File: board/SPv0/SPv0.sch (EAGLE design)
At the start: 53 parts, among them IC1 S34ML0XG1, IC2 F55[0/1]X---PT48, IC3 LM339D, Q1 12MHz, T1 n3904, T2 n3904, T3 n3906, T4 n3906, T5 n3906

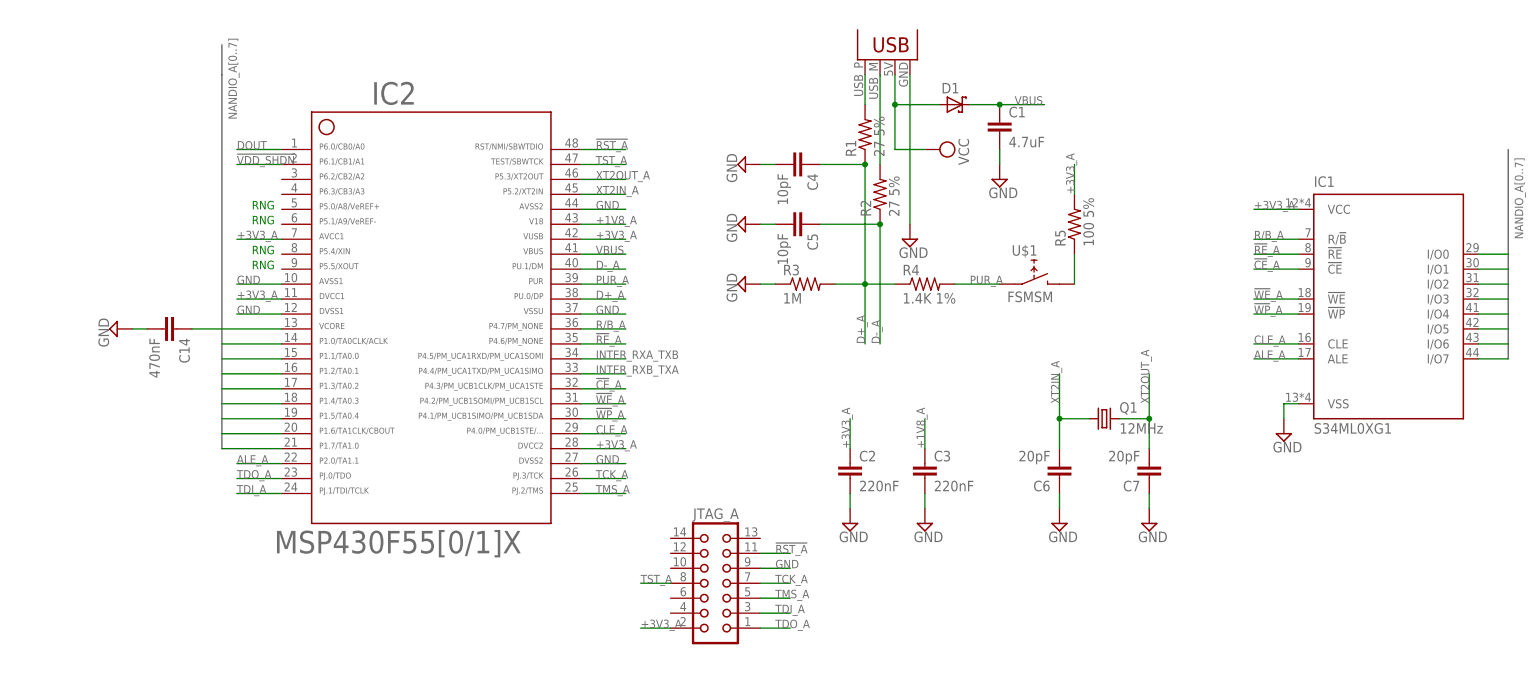
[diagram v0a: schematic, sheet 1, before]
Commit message: added own footprints for 0805 parts reorganizing board somewhat
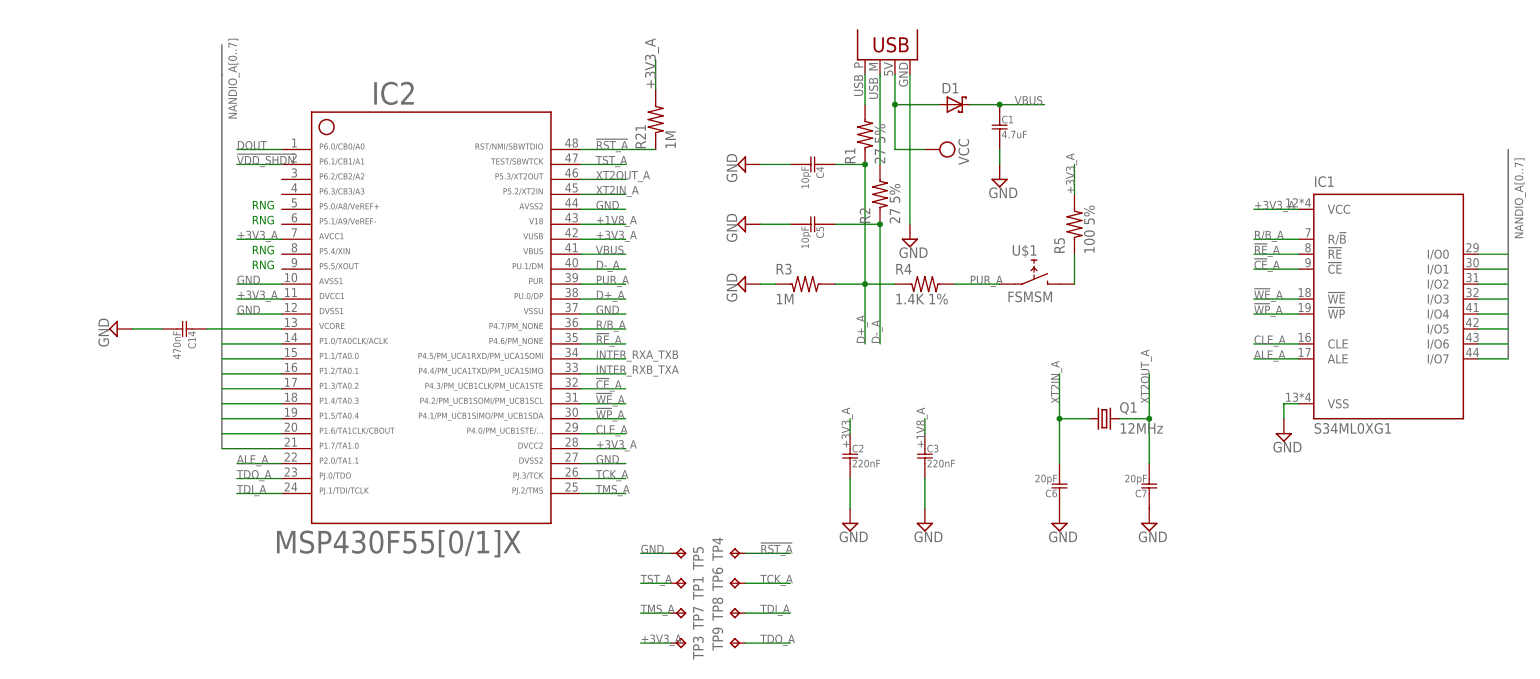
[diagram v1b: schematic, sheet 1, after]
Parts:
- removed JTAG_A: (no value), con-harting:CON14
- added R21: 1M, Passives:R0805
- added TP1, TP3, TP4, TP5, TP6, TP7, TP8, TP9: TPTP08SQ, testpad:TPTP08SQ
- C1, C14, C2, C3, C4, C5, C6, C7: device rcl:C-EUC0805 -> Passives:C0805
- Q1: device Passives:CRYSTAL -> Passives:CRYSTALCSM-3X
- R1, R2, R3, R4, R5: device rcl:R-US_R0805 -> Passives:R0805
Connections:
- net !RST_A!: now also R21.1, TP4.TP; no longer JTAG_A.11
- net +3V3_A: now also R21.2, TP3.TP; no longer JTAG_A.2
- net GND: now also TP5.TP; no longer JTAG_A.9
- net TCK_A: now also TP6.TP; no longer JTAG_A.7
- net TDI_A: now also TP8.TP; no longer JTAG_A.3
- net TDO_A: now also TP9.TP; no longer JTAG_A.1
- net TMS_A: now also TP7.TP; no longer JTAG_A.5
- net TST_A: now also TP1.TP; no longer JTAG_A.8

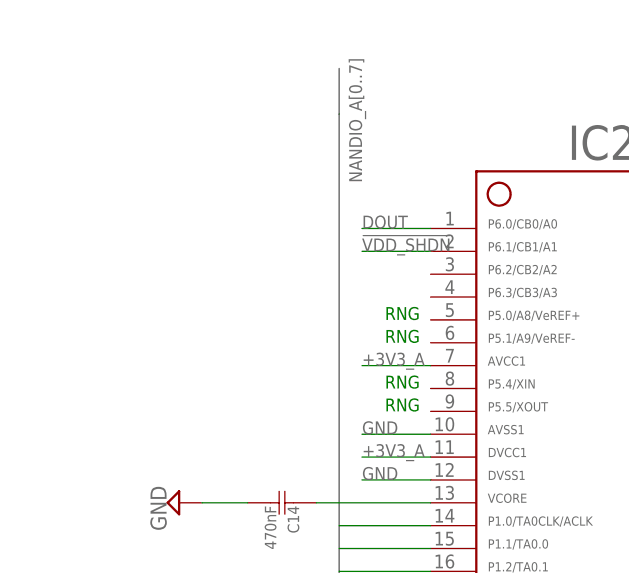
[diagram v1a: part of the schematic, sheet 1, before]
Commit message: adding primordial hwrng support added leds to library, board
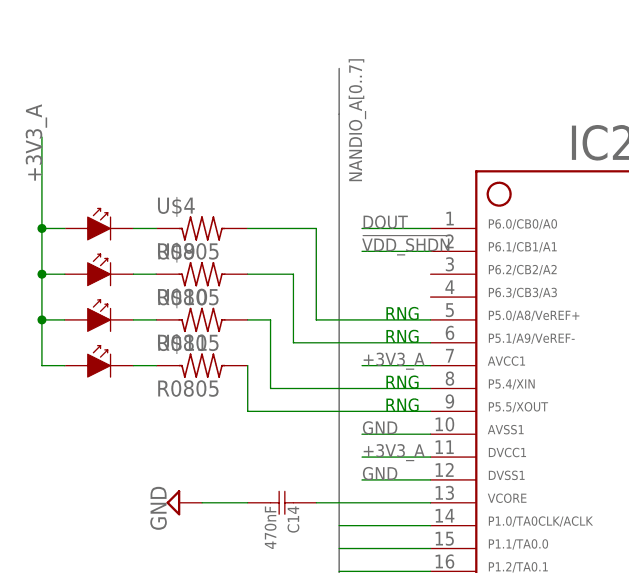
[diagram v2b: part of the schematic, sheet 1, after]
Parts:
- added U$10, U$11, U$4, U$9: R0805, Passives:R0805
- added U$5, U$6, U$7, U$8: LED, Passives:LED
- D2, D3: value (none) -> 1n4148
- IC3: value LM339D -> TL084D; device linear:LM339D -> linear:TL084D
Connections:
- new net N$19: IC2.9, U$11.2
- new net N$22: U$10.1, U$7.CATHODE
- new net N$23: U$6.CATHODE, U$9.1
- new net N$24: U$4.1, U$5.CATHODE
- new net N$25: U$11.1, U$8.CATHODE
- new net N$26: IC2.8, U$10.2
- new net N$27: IC2.6, U$9.2
- new net N$28: IC2.5, U$4.2
- net +3V3_A: now also U$5.ANODE, U$6.ANODE, U$7.ANODE, U$8.ANODE
- net GND: now also IC3P.V-; no longer IC3P.GND
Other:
- moved on the sheet: IC3C
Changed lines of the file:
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@@
 <part name="R7" library="rcl" deviceset="R-US_" device="R0603" value="1M"/>
 <part name="SUPPLY11" library="supply2" deviceset="GND" device=""/>
-<part name="IC3" library="linear" deviceset="LM339" device="D"/>
+<part name="IC3" library="linear" deviceset="TL084" device="D"/>
 <part name="C8" library="rcl" deviceset="C-EU" device="C0805" value="0.47u"/>
 <part name="C9" library="rcl" deviceset="C-EU" device="C0805" value="0.47u"/>
@@
 <part name="R16" library="rcl" deviceset="R-US_" device="R0603" value="5K"/>
 <part name="R17" library="rcl" deviceset="R-US_" device="R0603" value="5K"/>
-<part name="D2" library="zetex" deviceset="D" device="SOD323"/>
-<part name="D3" library="zetex" deviceset="D" device="SOD323"/>
+<part name="D2" library="zetex" deviceset="D" device="SOD323" value="1n4148"/>
+<part name="D3" library="zetex" deviceset="D" device="SOD323" value="1n4148"/>
 <part name="SUPPLY14" library="supply2" deviceset="GND" device=""/>
 <part name="SUPPLY15" library="supply2" deviceset="GND" device=""/>
@@
 <part name="TP9" library="testpad" deviceset="TP" device="TP08SQ"/>
 <part name="R21" library="Passives" deviceset="R" device="0805" value="1M"/>
+<part name="U$5" library="Passives" deviceset="LED" device=""/>
+<part name="U$6" library="Passives" deviceset="LED" device=""/>
+<part name="U$7" library="Passives" deviceset="LED" device=""/>
+<part name="U$8" library="Passives" deviceset="LED" device=""/>
+<part name="U$4" library="Passives" deviceset="R" device="0805"/>
+<part name="U$9" library="Passives" deviceset="R" device="0805"/>
+<part name="U$10" library="Passives" deviceset="R" device="0805"/>
+<part name="U$11" library="Passives" deviceset="R" device="0805"/>
 </parts>
 <sheets>
@@
 <instance part="TP9" gate="G$1" x="99.06" y="33.02" rot="R90"/>
 <instance part="R21" gate="G$1" x="86.36" y="121.92" rot="R90"/>
+<instance part="U$5" gate="G$1" x="-12.7" y="116.84"/>
+<instance part="U$6" gate="G$1" x="-12.7" y="111.76"/>
+<instance part="U$7" gate="G$1" x="-12.7" y="106.68"/>
+<instance part="U$8" gate="G$1" x="-12.7" y="101.6"/>
+<instance part="U$4" gate="G$1" x="-2.54" y="116.84"/>
+<instance part="U$9" gate="G$1" x="-2.54" y="111.76"/>
+<instance part="U$10" gate="G$1" x="-2.54" y="106.68"/>
+<instance part="U$11" gate="G$1" x="-2.54" y="101.6"/>
 </instances>
 <busses>
@@
 <wire x1="86.36" y1="127" x2="86.36" y2="132.08" width="0.1524" layer="91"/>
 <label x="86.36" y="127" size="1.778" layer="95" rot="R90"/>
+</segment>
+<segment>
+<pinref part="U$8" gate="G$1" pin="ANODE"/>
+<wire x1="-17.78" y1="101.6" x2="-20.32" y2="101.6" width="0.1524" layer="91"/>
+<wire x1="-20.32" y1="101.6" x2="-20.32" y2="106.68" width="0.1524" layer="91"/>
+<pinref part="U$5" gate="G$1" pin="ANODE"/>
+<wire x1="-20.32" y1="106.68" x2="-20.32" y2="111.76" width="0.1524" layer="91"/>
+<wire x1="-20.32" y1="111.76" x2="-20.32" y2="116.84" width="0.1524" layer="91"/>
+<wire x1="-20.32" y1="116.84" x2="-20.32" y2="127" width="0.1524" layer="91"/>
+<wire x1="-17.78" y1="116.84" x2="-20.32" y2="116.84" width="0.1524" layer="91"/>
+<junction x="-20.32" y="116.84"/>
+<pinref part="U$6" gate="G$1" pin="ANODE"/>
+<wire x1="-17.78" y1="111.76" x2="-20.32" y2="111.76" width="0.1524" layer="91"/>
+<junction x="-20.32" y="111.76"/>
+<pinref part="U$7" gate="G$1" pin="ANODE"/>
+<wire x1="-17.78" y1="106.68" x2="-20.32" y2="106.68" width="0.1524" layer="91"/>
+<junction x="-20.32" y="106.68"/>
+<label x="-20.32" y="121.92" size="1.778" layer="95" rot="R90"/>
 </segment>
 </net>
@@
 <wire x1="22.86" y1="114.3" x2="15.24" y2="114.3" width="0.1524" layer="91"/>
 <label x="15.24" y="114.3" size="1.4224" layer="95"/>
+</segment>
+</net>
+<net name="N$22" class="0">
+<segment>
+<pinref part="U$7" gate="G$1" pin="CATHODE"/>
+<pinref part="U$10" gate="G$1" pin="1"/>
+<wire x1="-10.16" y1="106.68" x2="-7.62" y2="106.68" width="0.1524" layer="91"/>
+</segment>
+</net>
+<net name="N$23" class="0">
+<segment>
+<pinref part="U$6" gate="G$1" pin="CATHODE"/>
+<pinref part="U$9" gate="G$1" pin="1"/>
+<wire x1="-10.16" y1="111.76" x2="-7.62" y2="111.76" width="0.1524" layer="91"/>
+</segment>
+</net>
+<net name="N$24" class="0">
+<segment>
+<pinref part="U$5" gate="G$1" pin="CATHODE"/>
+<pinref part="U$4" gate="G$1" pin="1"/>
+<wire x1="-10.16" y1="116.84" x2="-7.62" y2="116.84" width="0.1524" layer="91"/>
+</segment>
+</net>
+<net name="N$25" class="0">
+<segment>
+<pinref part="U$8" gate="G$1" pin="CATHODE"/>
+<pinref part="U$11" gate="G$1" pin="1"/>
+<wire x1="-10.16" y1="101.6" x2="-7.62" y2="101.6" width="0.1524" layer="91"/>
+</segment>
+</net>
+<net name="N$19" class="0">
+<segment>
+<pinref part="U$11" gate="G$1" pin="2"/>
+<wire x1="2.54" y1="101.6" x2="2.54" y2="96.52" width="0.1524" layer="91"/>
+<pinref part="IC2" gate="G$1" pin="9"/>
+<wire x1="2.54" y1="96.52" x2="22.86" y2="96.52" width="0.1524" layer="91"/>
+</segment>
+</net>
+<net name="N$26" class="0">
+<segment>
+<pinref part="IC2" gate="G$1" pin="8"/>
+<wire x1="22.86" y1="99.06" x2="5.08" y2="99.06" width="0.1524" layer="91"/>
+<wire x1="5.08" y1="99.06" x2="5.08" y2="106.68" width="0.1524" layer="91"/>
+<pinref part="U$10" gate="G$1" pin="2"/>
+<wire x1="5.08" y1="106.68" x2="2.54" y2="106.68" width="0.1524" layer="91"/>
+</segment>
+</net>
+<net name="N$27" class="0">
+<segment>
+<pinref part="U$9" gate="G$1" pin="2"/>
+<wire x1="2.54" y1="111.76" x2="7.62" y2="111.76" width="0.1524" layer="91"/>
+<wire x1="7.62" y1="111.76" x2="7.62" y2="104.14" width="0.1524" layer="91"/>
+<pinref part="IC2" gate="G$1" pin="6"/>
+<wire x1="7.62" y1="104.14" x2="22.86" y2="104.14" width="0.1524" layer="91"/>
+</segment>
+</net>
+<net name="N$28" class="0">
+<segment>
+<pinref part="U$4" gate="G$1" pin="2"/>
+<wire x1="2.54" y1="116.84" x2="10.16" y2="116.84" width="0.1524" layer="91"/>
+<wire x1="10.16" y1="116.84" x2="10.16" y2="106.68" width="0.1524" layer="91"/>
+<pinref part="IC2" gate="G$1" pin="5"/>
+<wire x1="10.16" y1="106.68" x2="22.86" y2="106.68" width="0.1524" layer="91"/>
 </segment>
 </net>
@@
 </segment>
 <segment>
-<pinref part="IC3" gate="P" pin="GND"/>
+<pinref part="IC3" gate="P" pin="V-"/>
 <wire x1="172.72" y1="22.86" x2="172.72" y2="20.32" width="0.1524" layer="91"/>
 <pinref part="SUPPLY17" gate="GND" pin="GND"/>

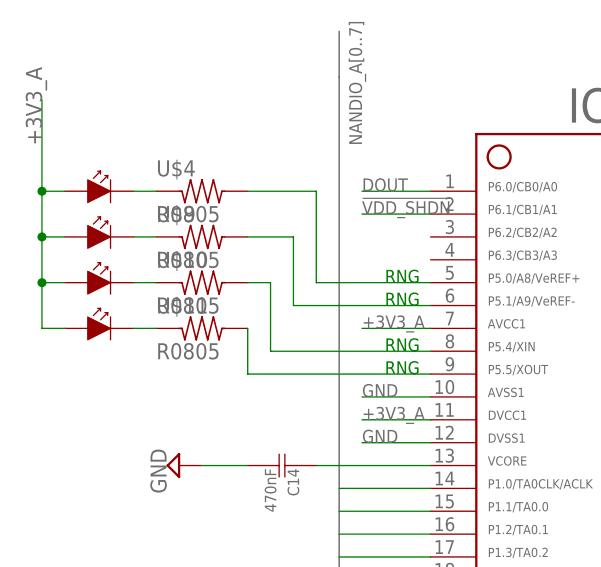
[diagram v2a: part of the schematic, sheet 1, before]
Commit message: added LEDs, starting layout
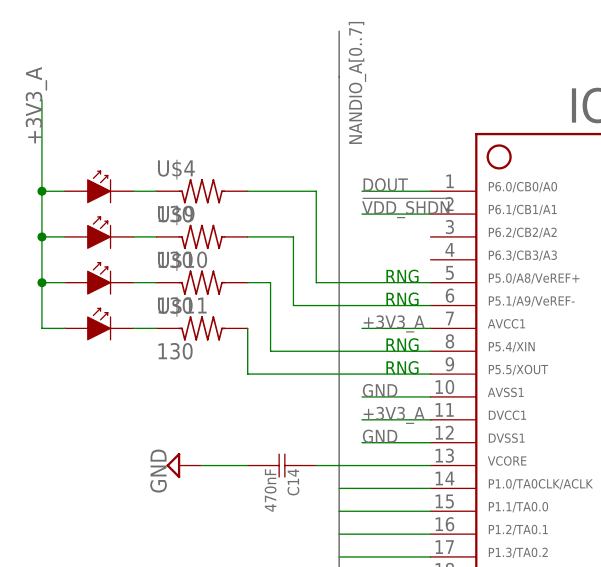
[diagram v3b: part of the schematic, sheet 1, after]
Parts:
- U$10, U$11, U$4, U$9: value R0805 -> 130
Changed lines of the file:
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@@
 <part name="U$7" library="Passives" deviceset="LED" device=""/>
 <part name="U$8" library="Passives" deviceset="LED" device=""/>
-<part name="U$4" library="Passives" deviceset="R" device="0805"/>
-<part name="U$9" library="Passives" deviceset="R" device="0805"/>
-<part name="U$10" library="Passives" deviceset="R" device="0805"/>
-<part name="U$11" library="Passives" deviceset="R" device="0805"/>
+<part name="U$4" library="Passives" deviceset="R" device="0805" value="130"/>
+<part name="U$9" library="Passives" deviceset="R" device="0805" value="130"/>
+<part name="U$10" library="Passives" deviceset="R" device="0805" value="130"/>
+<part name="U$11" library="Passives" deviceset="R" device="0805" value="130"/>
 </parts>
 <sheets>
